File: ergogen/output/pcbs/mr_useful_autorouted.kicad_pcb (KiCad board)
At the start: 2 copper layers, 57 x 95 mm, 37 parts

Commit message: Add JLCPCB order number text
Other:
- board text added: "JLCJLCJLCJLC"
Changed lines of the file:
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@@
   (general
     (thickness 1.6)
-    (drawings 8)
+    (drawings 9)
     (tracks 444)
     (zones 0)
@@
       (xy 10.839479 -6.37476) (xy 10.012656 -6.37476) (xy -9.485812 -6.37476)) (layer F.SilkS) (width 0.01))
   )
+  (gr_text JLCJLCJLCJLC (at 79 87) (layer B.SilkS)
+    (effects (font (size 1 1) (thickness 0.15)) (justify mirror))
+  )
   (gr_line (start 51.5 134.5) (end 106.5 134.5) (angle 90) (layer Edge.Cuts) (width 0.15))

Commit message: Update assets
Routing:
- net ULED_4: track 87.1 -> 64.1 mm, vias 4 -> 2
- net R0: track 121.8 -> 130.6 mm, vias 1 -> 0
- net ULED_2: track 35.0 -> 27.2 mm, vias 2 -> 0
- net left_down: track 11.2 -> 3.46 mm
- net VCC: track 303.3 -> 296.1 mm
- net LED_6: track 45.3 -> 39.4 mm
- net C0: track 115.1 -> 109.3 mm
- net GND: track 272.2 -> 277.7 mm
- net ULED_3: track 63.0 -> 68.3 mm
- net R3: track 60.4 -> 64.6 mm, vias 1 -> 3
- net R4: track 45.6 -> 42.9 mm
- net C1: track 89.4 -> 87.3 mm
- net LED_8: track 33.8 -> 32.4 mm
- net LED_9: track 73.6 -> 72.4 mm
- net ULED_1: track 23.2 -> 23.8 mm
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
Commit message: Update assets
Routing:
- net LED_6: track 39.4 -> 77.0 mm
- net VCC: track 296.1 -> 318.8 mm, vias 4 -> 3
- net GND: track 277.7 -> 299.6 mm, vias 5 -> 4
- net ULED_4: track 64.1 -> 47.4 mm
- net R3: track 64.6 -> 57.3 mm, vias 3 -> 1
- net R0: track 130.6 -> 137.6 mm, vias 0 -> 1
- net ULED_3: track 68.3 -> 62.7 mm
- net LED_5: track 23.5 -> 19.8 mm
- net LED_9: track 72.4 -> 69.0 mm
- net LED_3: track 67.5 -> 70.8 mm
- net LED_2: track 28.8 -> 31.7 mm, vias 2 -> 0
- net R1: track 67.7 -> 65.1 mm, vias 2 -> 1
- net LED_7: track 25.0 -> 27.3 mm
- net R4: track 42.9 -> 45.0 mm
- net ULED_2: track 27.2 -> 28.9 mm, vias 0 -> 2
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
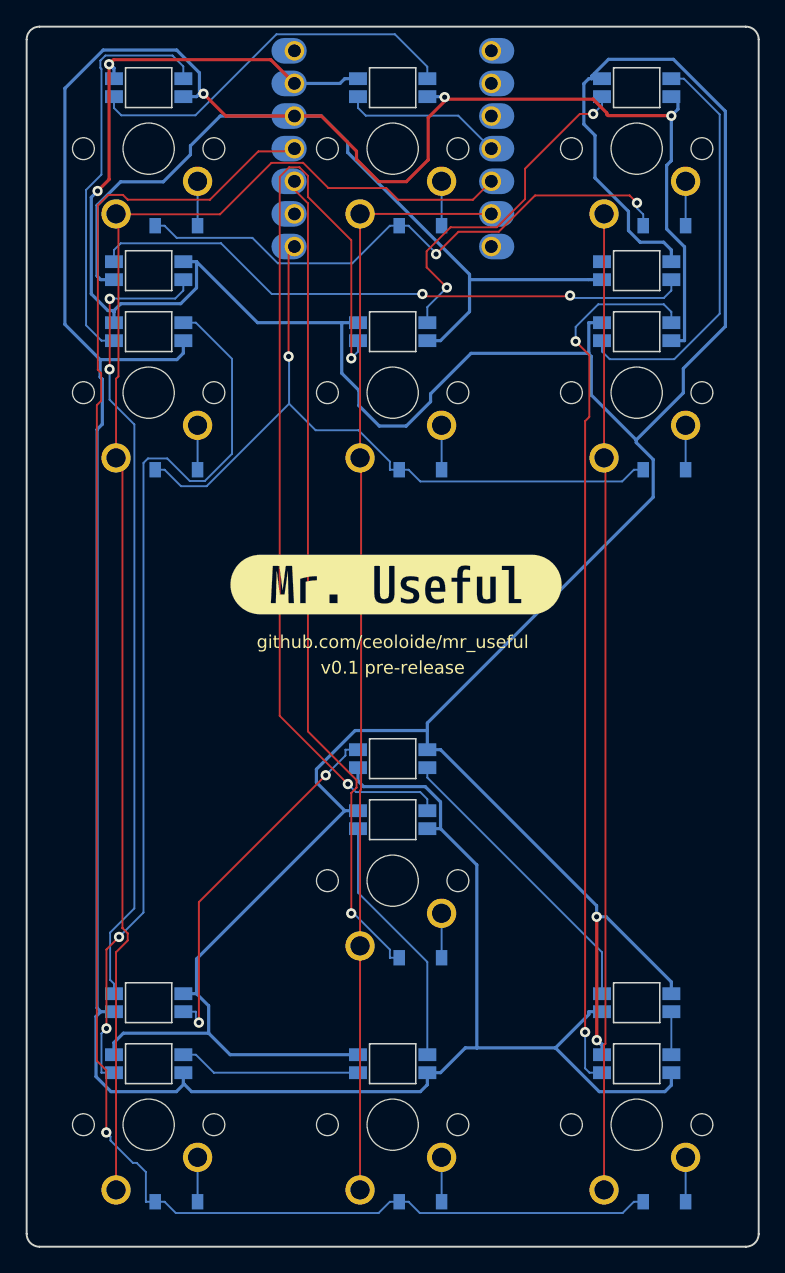
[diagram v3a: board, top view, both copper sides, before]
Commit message: Update rules with fixes and new defaults
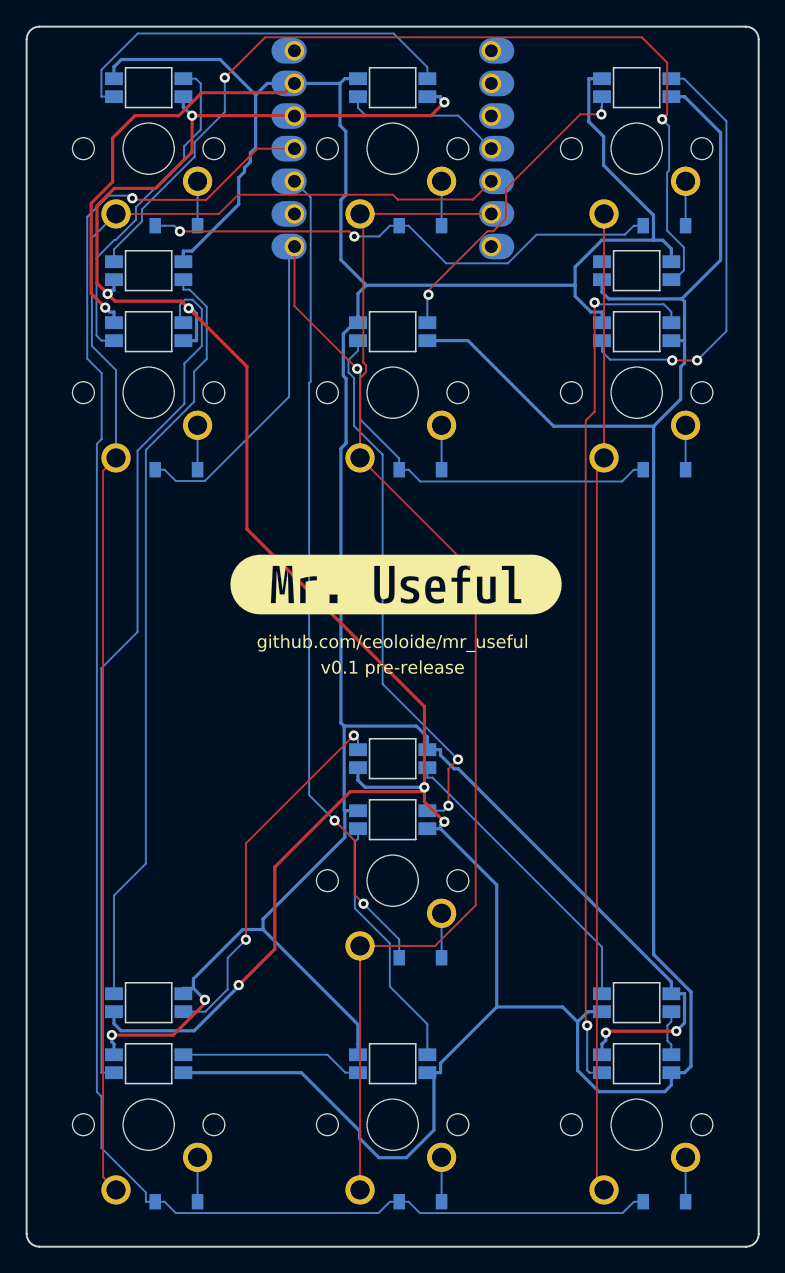
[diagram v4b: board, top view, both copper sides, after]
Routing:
- net LED_6: track 77.0 -> 42.2 mm
- net GND: track 299.6 -> 269.1 mm, vias 4 -> 5
- net ULED_4: track 47.4 -> 72.9 mm
- net VCC: track 318.8 -> 333.7 mm, vias 3 -> 7
- net C1: track 86.7 -> 97.8 mm
- net R3: track 57.3 -> 66.1 mm
- net LED_2: track 31.7 -> 26.1 mm
- net R4: track 45.0 -> 41.1 mm
- net LED_3: track 70.8 -> 67.4 mm, vias 2 -> 0
- net ULED_3: track 62.7 -> 59.6 mm, vias 2 -> 0
- net LED_7: track 27.3 -> 24.5 mm
- net LED_8: track 32.2 -> 33.8 mm, vias 0 -> 2
- net LED_1: track 30.1 -> 31.6 mm
- net R1: track 65.1 -> 64.4 mm, vias 1 -> 2
- net LED_9: track 69.0 -> 68.5 mm
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
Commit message: Update assets
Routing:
- net VCC: track 333.7 -> 291.1 mm
- net ULED_2: track 29.2 -> 0.00 mm, vias 2 -> 0
- net ULED_4: track 72.9 -> 47.1 mm
- net C2: track 76.5 -> 93.4 mm
- net LED_6: track 42.2 -> 54.5 mm
- net R0: track 138.1 -> 148.2 mm
- net R1: track 64.4 -> 72.7 mm
- net GND: track 269.1 -> 260.8 mm
- net ULED_3: track 59.6 -> 65.4 mm, vias 0 -> 2
- net R3: track 66.1 -> 60.7 mm, vias 1 -> 3
- net LED_8: track 33.8 -> 30.2 mm
- net C1: track 97.8 -> 101.1 mm, vias 0 -> 2
- net LED_9: track 68.5 -> 70.6 mm
- net LED_3: track 67.4 -> 65.7 mm
- net R4: track 41.1 -> 40.2 mm, vias 2 -> 3
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
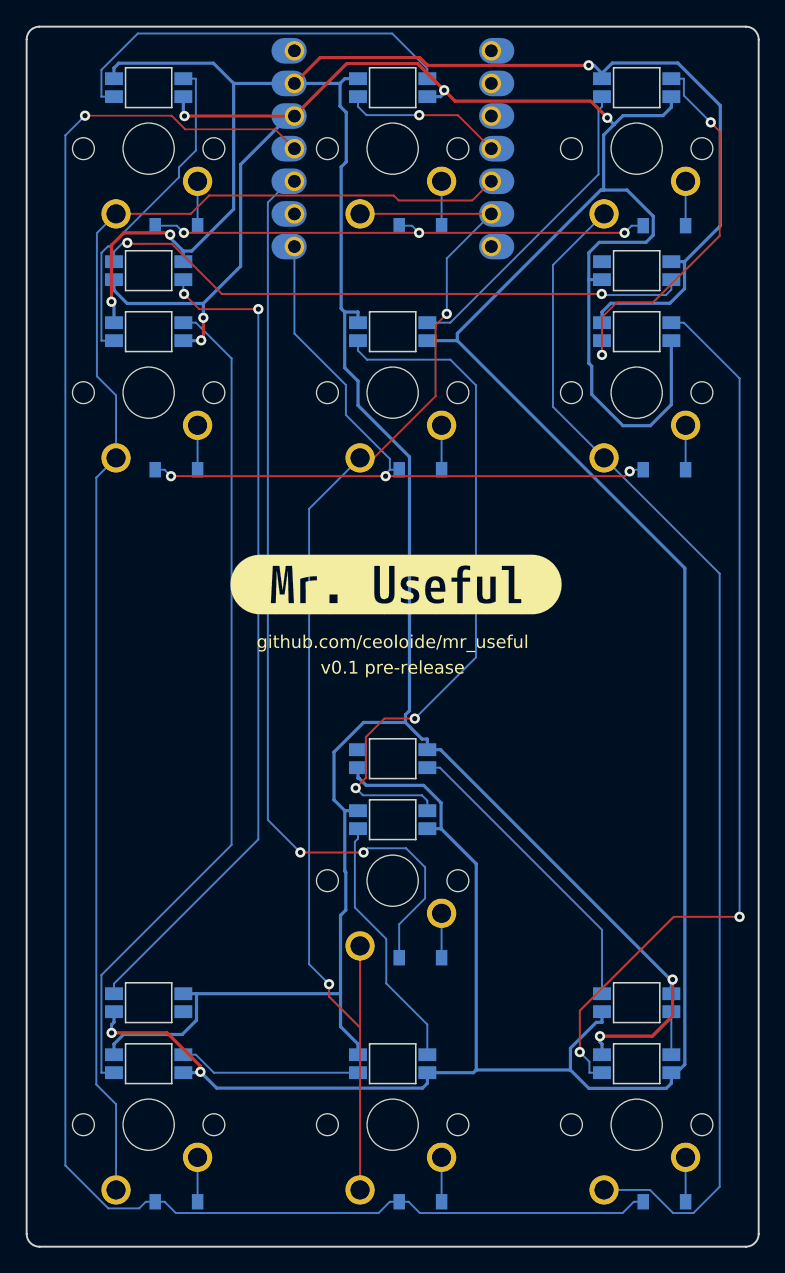
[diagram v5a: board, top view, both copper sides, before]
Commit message: Revert to Freerouting 1.0.0 CLI
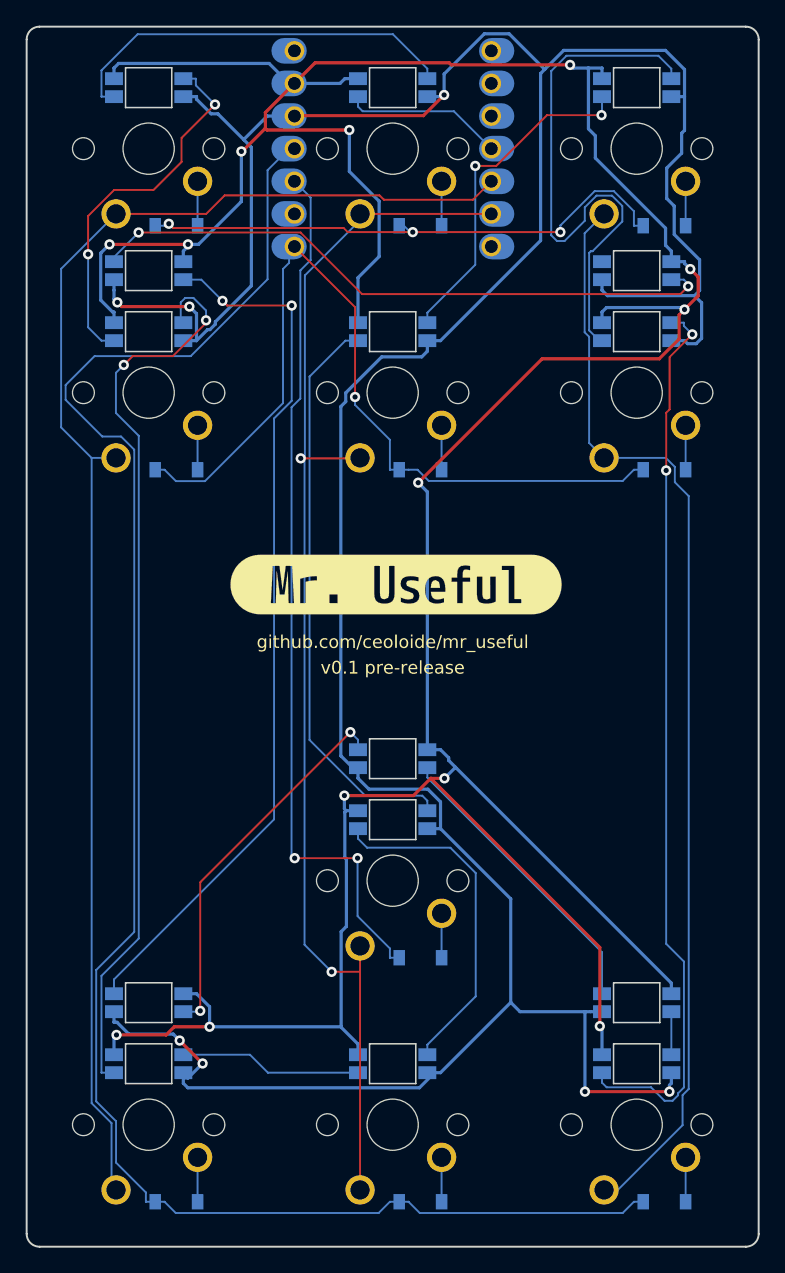
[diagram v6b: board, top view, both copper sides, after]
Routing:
- net ULED_2: track 0.00 -> 29.5 mm, vias 0 -> 2
- net GND: track 260.8 -> 289.4 mm, vias 5 -> 13
- net VCC: track 291.1 -> 266.6 mm
- net LED_8: track 30.2 -> 44.1 mm, vias 2 -> 0
- net LED_6: track 54.5 -> 45.1 mm, vias 2 -> 0
- net R0: track 148.2 -> 140.1 mm, vias 1 -> 0
- net C2: track 93.4 -> 86.2 mm
- net LED_5: track 20.0 -> 26.8 mm
- net R3: track 60.7 -> 66.5 mm, vias 3 -> 1
- net LED_3: track 65.7 -> 71.2 mm, vias 0 -> 2
- net R1: track 72.7 -> 68.8 mm
- net LED_2: track 25.5 -> 29.3 mm, vias 0 -> 2
- net ULED_3: track 65.4 -> 68.6 mm
- net C0: track 109.5 -> 112.4 mm
- net R4: track 40.2 -> 43.0 mm
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
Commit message: Update assets
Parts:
- D1, D10, D2, D3, D4, D5, D6, D7, D8, D9: footprint ComboDiode -> ceoloide:diode_tht_sod123
- LED1, LED10, LED2, LED3, LED4, LED5, LED6, LED7, LED8, LED9: footprint ceoloide:YS-SK6812MINI-E (per-key) -> ceoloide:led_SK6812mini-e (per-keysingle-side)
- LED11, LED12, LED13, LED14, LED15: footprint ceoloide:YS-SK6812MINI-E (underglow) -> ceoloide:led_SK6812mini-e (underglowsingle-side)
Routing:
- net GND: track 289.4 -> 258.5 mm, vias 13 -> 6
- net ULED_2: track 29.5 -> 46.9 mm
- net VCC: track 266.6 -> 282.6 mm, vias 7 -> 6
- net R0: track 140.1 -> 124.3 mm, vias 0 -> 1
- net LED_8: track 44.1 -> 32.2 mm
- net C1: track 98.5 -> 86.6 mm, vias 2 -> 0
- net ULED_3: track 68.6 -> 57.8 mm
- net C2: track 86.2 -> 76.7 mm
- net R3: track 66.5 -> 58.8 mm
- net LED_5: track 26.8 -> 19.8 mm
- net LED_9: track 70.5 -> 64.3 mm
- net LED_3: track 71.2 -> 66.0 mm
- net R1: track 68.8 -> 65.5 mm, vias 2 -> 1
- net ULED_4: track 49.7 -> 46.8 mm, vias 2 -> 0
- net LED_2: track 29.3 -> 27.2 mm
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
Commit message: Update assets
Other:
- net class Default removed
